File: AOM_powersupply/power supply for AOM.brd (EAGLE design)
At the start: 28 x 28 mm, 16 parts, among them IC1 TL071P

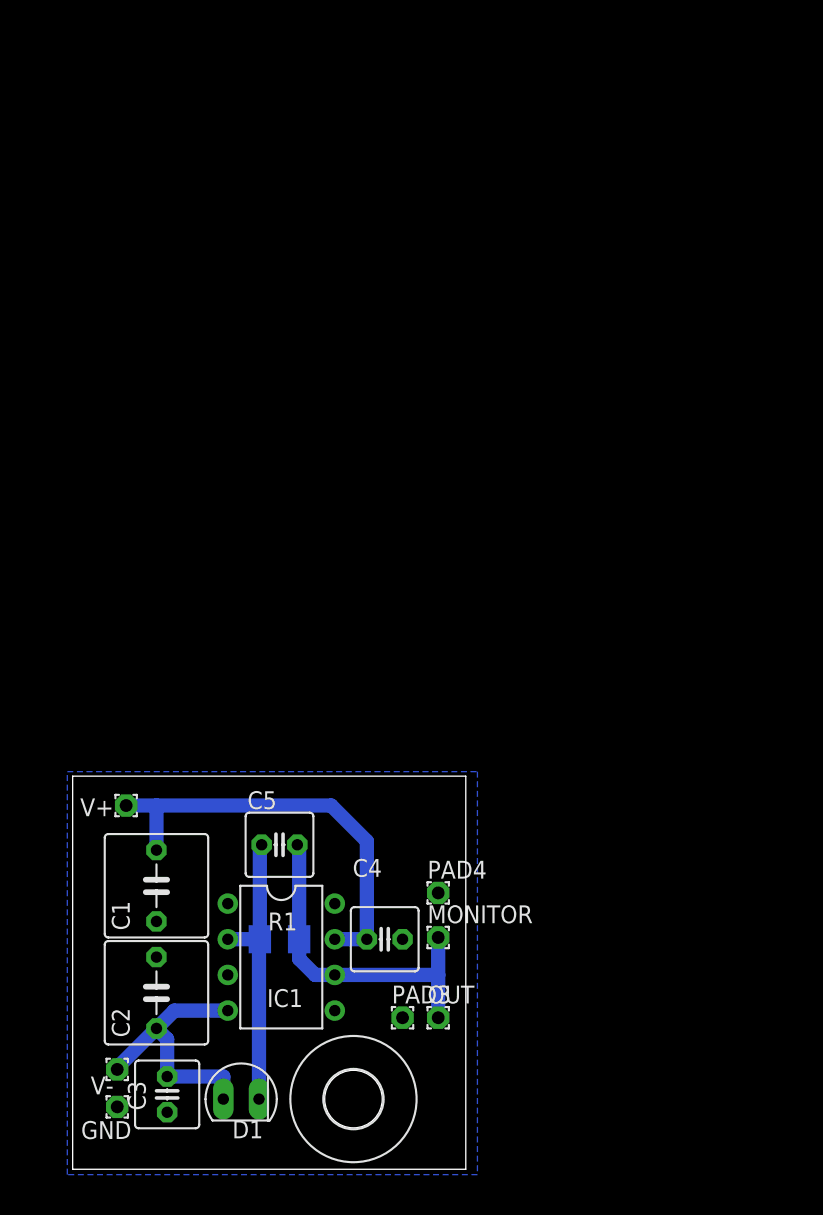
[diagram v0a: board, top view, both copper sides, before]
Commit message: added the shutter board and the AOM power supply by Pra
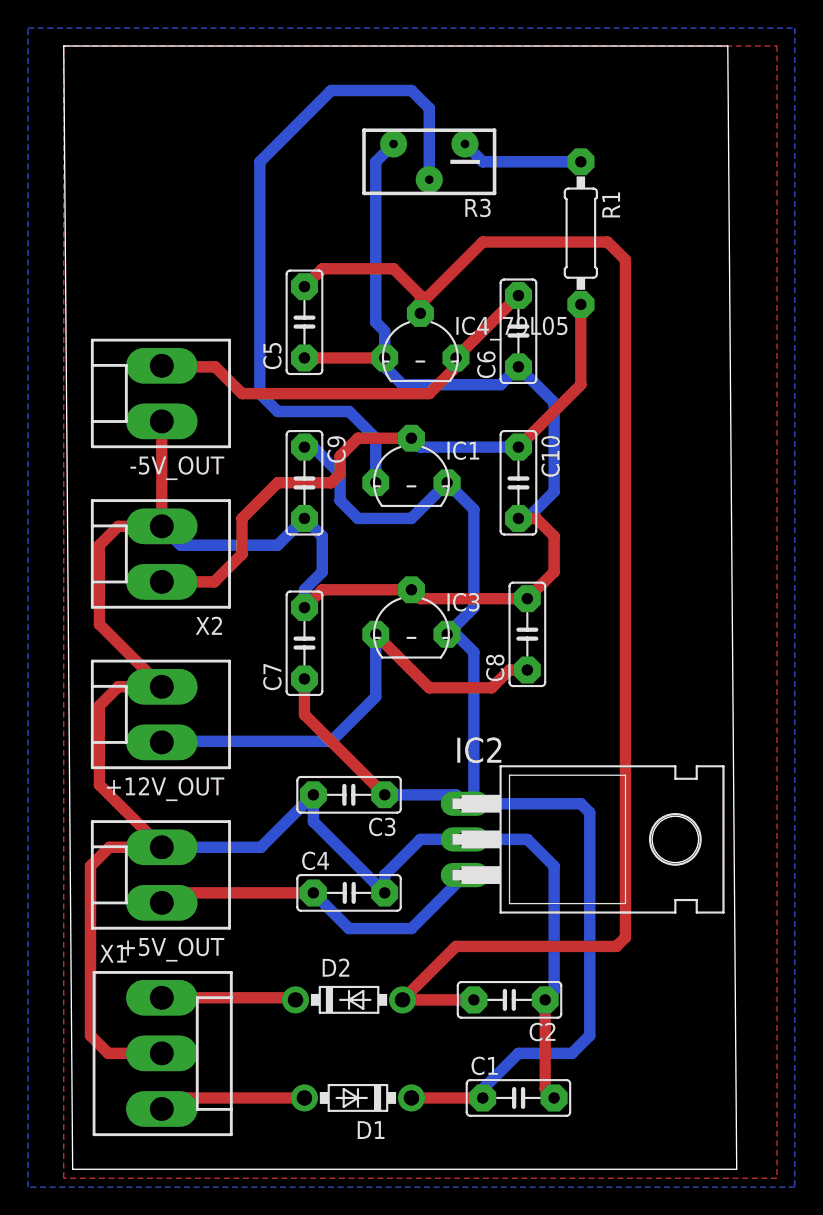
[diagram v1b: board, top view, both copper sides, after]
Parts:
- removed GND, MONITOR, OUT, PAD3, PAD4, V+, V-: (no value), wirepad:1,6/0,9
- removed H1: 4.1, holes:4,1
- added +12V_OUT, +5V_OUT, -5V_OUT, X2: (no value), con-molex:KK-156-2
- added C10, C6, C8: 10uF, rcl:C050-025X075
- added C7, C9: 1uF, rcl:C050-025X075
- added D2: 1N5817-B, diode:DO41-7.6
- added IC2: 7805T, linear:TO220H
- added IC3: 78L12Z, linear:TO92
- added IC4_79L05: (no value), linear:TO92
- added R3: (no value), rcl:RTRIM3296Y
- added X1: (no value), con-molex:KK-156-3
- C1, C2: value 2uF -> 47uF; device resistor:C050-075X075 -> rcl:C050-025X075
- C3: value 1nF -> 1uF; device resistor:C025-050X050 -> rcl:C050-025X075
- C4: value 1nF -> 10uF; device resistor:C025-050X050 -> rcl:C050-025X075
- C5: value 100pF -> 1uF; device resistor:C025-050X050 -> rcl:C050-025X075
- D1: value SFH206 -> 1N5817-B; device opto-trans-siemens:SFH206 -> diode:DO41-7.6
- IC1: value TL071P -> LM317LZ; device linear:DIL08 -> linear:TO92
- R1: value 10k -> 150; device resistor:M1206 -> rcl:0207/10
- moved R1 54.7 mm to (36.2, 66.7), flipped to the top, turned to 270 degrees
- moved C5 37.3 mm to (16.5, 60.3), turned to 90 degrees
- moved IC1 35.0 mm to (24.1, 48.9), turned to 0 degrees
- moved C1 29.9 mm to (31.8, 5.08), turned to 0 degrees
- moved C2 25.2 mm to (31.1, 12.1), turned to 180 degrees
- moved C3 25.0 mm to (19.7, 26.7), turned to 180 degrees
- moved D1 8.32 mm to (20.3, 5.08), turned to 180 degrees
- moved C4 4.17 mm to (19.7, 19.7)
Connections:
- removed net V+: C1.2, C4.1, IC1.7, V+.1
- removed net V-: C2.1, C3.1, D1.A, IC1.4, V-.1
- new net +24V: C1.1, C3.1, C7.1, C9.1, D1.C, IC1.3, IC2.1, IC3.3
- new net -24V: C2.2, C5.2, D2.A, IC4_79L05.2
- new net N$1: D2.C, X1.1
- new net N$4: +5V_OUT.1, C4.1, IC2.3
- new net N$5: -5V_OUT.2, C6.2, IC4_79L05.3
- new net N$6: R1.1, R3.1
- new net N$7: IC1.1, R3.2
- new net N$8: C10.1, IC1.2, R1.2, X2.1
- net GND: now also +12V_OUT.2, +5V_OUT.2, -5V_OUT.1, C1.2, C10.2, C2.1, C5.1, C6.1, C7.2, C8.2, C9.2, IC2.2, IC3.2, IC4_79L05.1, R3.3, X1.2, X2.2; no longer C1.1, C2.2, GND.1, IC1.3, PAD3.1, PAD4.1
- net N$2: now also D1.A, X1.3; no longer C5.2, IC1.6, MONITOR.1, OUT.1, R1.2
- net N$3: now also +12V_OUT.1, C8.1, IC3.1; no longer C5.1, D1.K, IC1.2, R1.1
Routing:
- net GND: track 0.00 -> 208.4 mm
- net -24V: track 0.00 -> 98.9 mm
- net +24V: track 0.00 -> 96.8 mm
- net N$7: track 0.00 -> 49.0 mm
- net N$8: track 0.00 -> 44.1 mm
- net V+: track 30.6 -> 0.00 mm
- net N$5: track 0.00 -> 29.5 mm
- net N$4: track 0.00 -> 24.5 mm
- net V-: track 19.4 -> 0.00 mm
- net N$2: track 24.3 -> 10.5 mm
- net N$3: track 20.5 -> 33.9 mm
- net N$1: track 0.00 -> 9.59 mm
- net N$6: track 0.00 -> 8.78 mm
- added copper zone on layer 1, net GND
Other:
- board size 28 x 28 mm -> 47.9 x 80 mm
